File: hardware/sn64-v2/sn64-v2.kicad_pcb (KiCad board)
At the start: 6 copper layers, 104 x 64 mm, 180 parts, among them J1 Riser joint 2x20 2.00mm, J101 DX07S016JA3R1500, J2 SNES cartridge socket 62, U1 LFE5U-85F-8BG381I, U10 TLV62569DBVR, U11 AP2112K-2.5TRG1, U12 TPS2553DBVR, U2 W25Q128JVSIQ, U201 SN74ALVC164245DGGR, U202 SN74ALVC164245DGGR, U203 SN74ALVC164245DGGR, U204 SN74ALVC164245DGGR, U205 SN74LVC07APWR, U3 TPS3808G01DBVR, U4 USBLC6-2SC6, U6 TLA2528IRTER, U7 TPS2121RUXR, U8 TPS63070RNMR, U9 TLV62569DBVR, X1 27MHz 1631-27005-BTBEYA

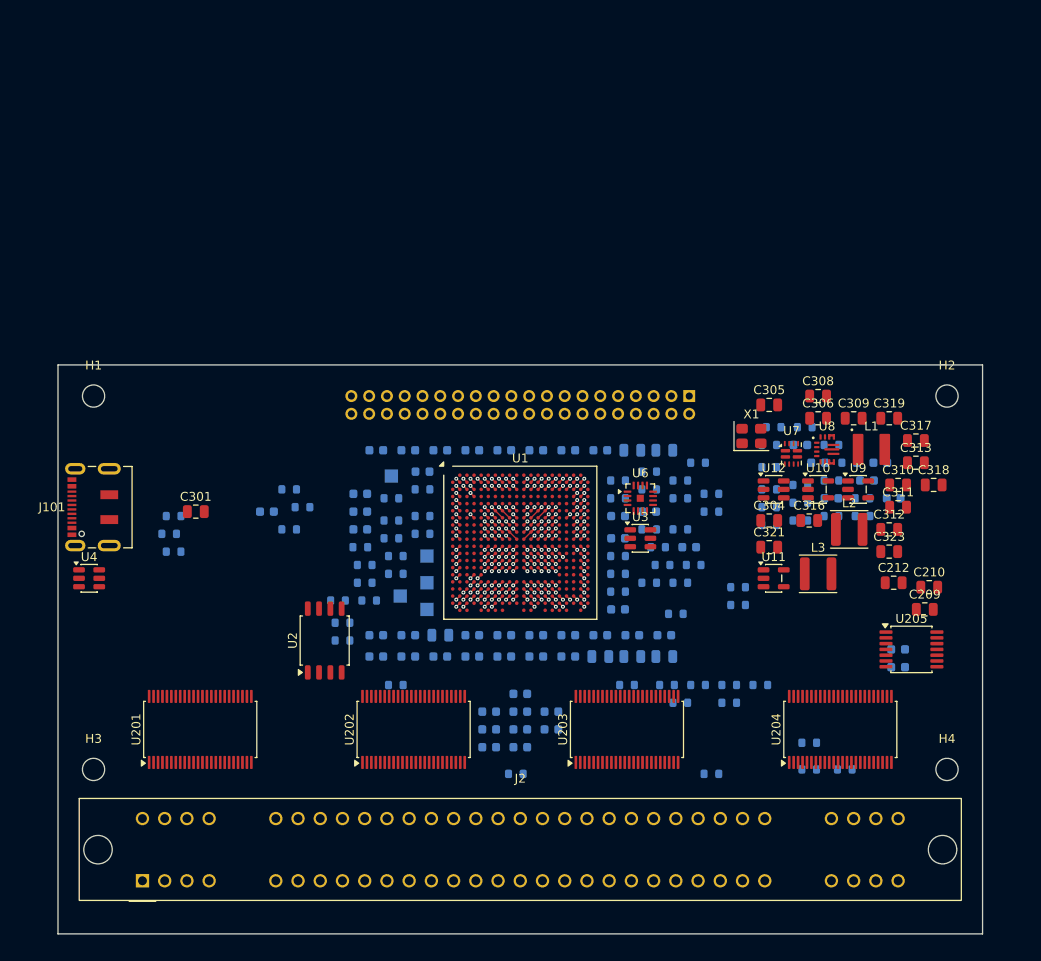
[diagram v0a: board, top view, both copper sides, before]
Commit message: v2 main board routed: 212/218 nets by one 40 s pass, planes and pours, DRC 0 errors; 7 hand items listed
Plane vias placed before routing (add_plane_vias_v2), 1.1 V island extended over its regulator on In4,
outer GND pours, renders and validation reports. Open items for hand routing in
hardware/sn64-v2/validation/pcb-open-connections.json. Work log and write-up updated.

Co-Authored-By: Claude Fable 5.1 <noreply@anthropic.com>
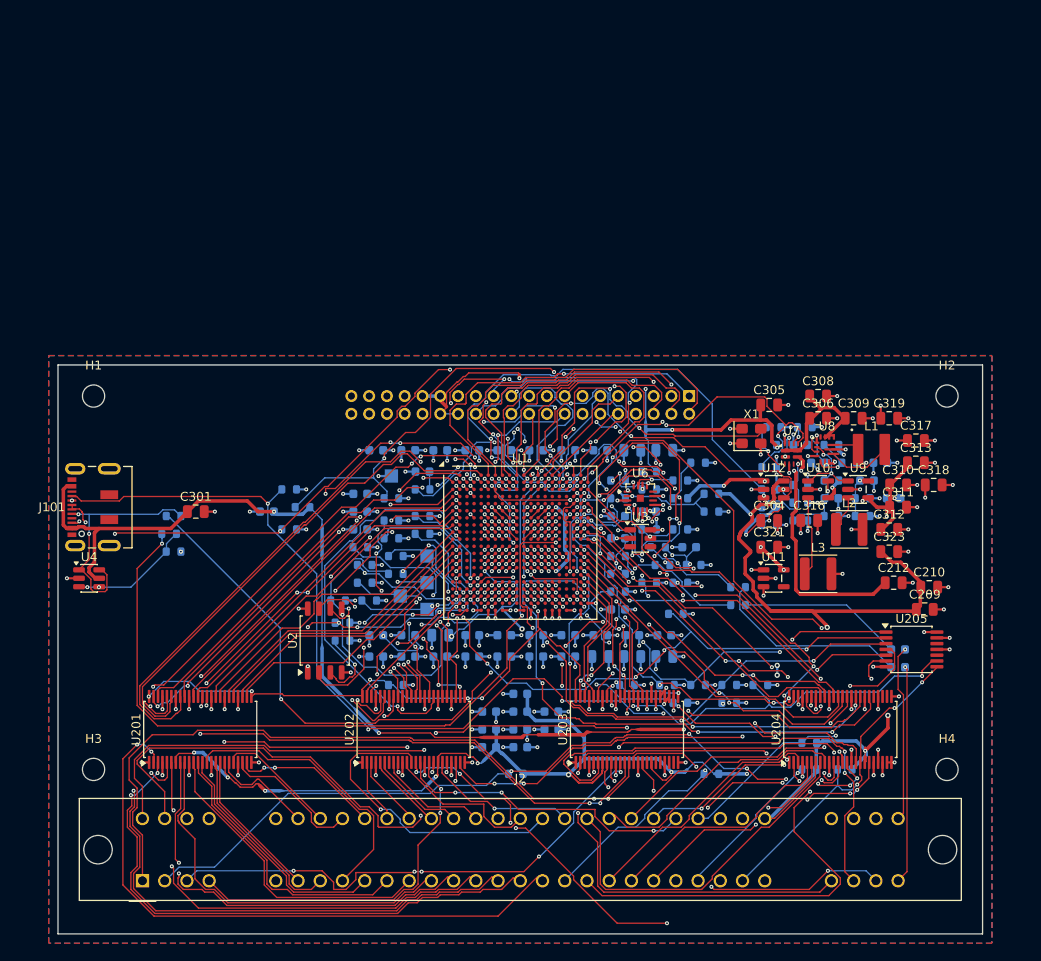
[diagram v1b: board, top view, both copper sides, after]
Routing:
- net SNES_5V_CART: track 0.00 -> 222.5 mm, vias 0 -> 12
- net GND: track 63.4 -> 261.4 mm, vias 94 -> 255
- net USB_VBUS: track 0.00 -> 143.6 mm, vias 0 -> 6
- net USB_CC2: track 0.00 -> 122.9 mm, vias 0 -> 7
- net FPGA_2V5: track 2.26 -> 111.2 mm, vias 4 -> 12
- net USB_CC1: track 0.00 -> 98.8 mm, vias 0 -> 12
- net FPGA_3V3: track 10.2 -> 104.7 mm, vias 18 -> 99
- net SNES_EXPAND: track 0.00 -> 91.1 mm, vias 0 -> 7
- net HOST_3V3: track 0.00 -> 88.9 mm, vias 0 -> 6
- net USB_DP_F: track 0.57 -> 87.9 mm, vias 1 -> 3
- net CTL_OE_N: track 0.57 -> 79.3 mm, vias 1 -> 7
- net SNES_SYSTEM_CLK: track 0.00 -> 78.1 mm, vias 0 -> 2
- net USB_DN_F: track 0.57 -> 77.3 mm, vias 1 -> 4
- net CIC_DATA0_OD: track 0.57 -> 72.2 mm, vias 1 -> 6
- net SNES_A0: track 0.00 -> 69.6 mm, vias 0 -> 2
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- added copper zone on B.Cu, net GND
- added copper zone on F.Cu, net GND

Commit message: v2 single board: routed board, schematic with the N64 edge, validation reports, renders and notes
Co-Authored-By: Claude Fable 5.1 <noreply@anthropic.com>
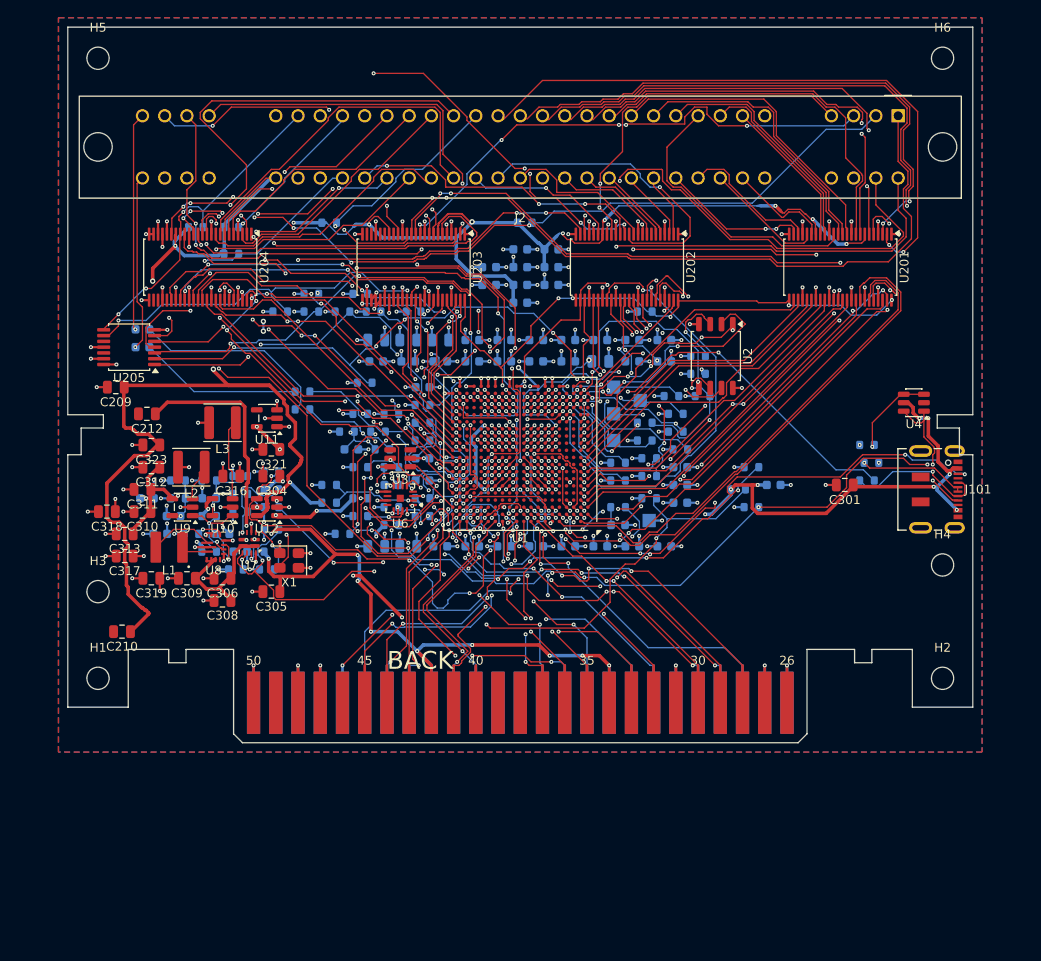
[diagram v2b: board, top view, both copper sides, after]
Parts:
- added H5: MountingHole_2.5mm, MountingHole_2.5mm, F.Cu at (-47.5, -66.5)
- added H6: MountingHole_2.5mm, MountingHole_2.5mm, F.Cu at (47.5, -66.5)
- J1: value Riser joint 2x20 2.00mm -> N64 cartridge edge; footprint PinSocket_2x20_P2.00mm_Vertical -> N64_Edge_SC64_Reference; moved to F.Cu
- moved R207 95.1 mm to (-36.5, -47.5), turned to 0 degrees
- moved U4 94.8 mm to (44.3, -27.8), turned to 180 degrees
- moved C209 94.4 mm to (-45.5, -29.5), turned to 180 degrees
- moved U205 94.3 mm to (-44.0, -34.0), turned to 180 degrees
- moved J101 93.6 mm to (46.2, -18.0), turned to -90 degrees
- moved C36 93.1 mm to (-42.5, -36.0), turned to 0 degrees
- moved C318 93.0 mm to (-46.5, -15.5), turned to 180 degrees
- moved C38 91.5 mm to (-42.5, -34.0), turned to 0 degrees
- moved C210 90.9 mm to (-44.8, -2.00), turned to 180 degrees
- moved C317 89.9 mm to (-44.5, -10.5), turned to 180 degrees
- moved C313 89.4 mm to (-44.5, -13.0), turned to 180 degrees
- moved R206 89.1 mm to (-32.5, -47.5), turned to 0 degrees
- moved U201 88.8 mm to (36.0, -43.0), turned to -90 degrees
- moved U204 88.8 mm to (-36.0, -43.0), turned to -90 degrees
- moved C212 86.1 mm to (-42.0, -26.5), turned to 180 degrees
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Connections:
- J1 pad 1: N64_AD0 -> GND
- J1 pad 10: N64_AD9 -> N64_READ_N
- J1 pad 11: N64_AD10 -> N64_AD11
- J1 pad 12: N64_AD11 -> N64_AD10
- J1 pad 13: N64_AD12 -> (no net)
- J1 pad 14: N64_AD13 -> (no net)
- J1 pad 15: N64_AD14 -> N64_AD9
- J1 pad 16: N64_AD15 -> N64_AD8
- J1 pad 17: N64_ALE_L -> HOST_3V3
- J1 pad 18: N64_ALE_H -> N64_CIC_DATA
- J1 pad 19: N64_READ_N -> N64_PIF_CLK
- J1 pad 2: N64_AD1 -> GND
- J1 pad 20: N64_WRITE_N -> N64_RESET_N
- J1 pad 21: N64_RESET_N -> N64_JOYBUS
- J1 pad 22: N64_NMI_N -> GND
- J1 pad 23: N64_INT_N -> GND
- J1 pad 24: N64_CIC_CLK -> (no net)
- J1 pad 25: N64_CIC_DATA -> GND
- J1 pad 26: N64_PIF_CLK -> GND
- J1 pad 27: N64_JOYBUS -> GND
- J1 pad 28: HOST_3V3 -> N64_AD0
- J1 pad 29: HOST_3V3 -> N64_AD1
- J1 pad 3: N64_AD2 -> N64_AD15
- J1 pad 30: HOST_3V3 -> N64_AD2
- J1 pad 31: HOST_3V3 -> GND
- J1 pad 32: GND -> N64_AD3
- J1 pad 33: GND -> N64_ALE_L
- J1 pad 34: GND -> HOST_3V3
- J1 pad 35: GND -> N64_ALE_H
- J1 pad 36: GND -> N64_AD4
- J1 pad 37: GND -> N64_AD5
- J1 pad 38: GND -> (no net)
- J1 pad 39: GND -> (no net)
- J1 pad 4: N64_AD3 -> N64_AD14
- J1 pad 40: GND -> N64_AD6
- J1 pad 5: N64_AD4 -> N64_AD13
- J1 pad 6: N64_AD5 -> GND
- J1 pad 7: N64_AD6 -> N64_AD12
- J1 pad 8: N64_AD7 -> N64_WRITE_N
- J1 pad 9: N64_AD8 -> HOST_3V3
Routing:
- net USB_DP_F: track 87.9 -> 0.00 mm, vias 3 -> 1
- net GND: track 261.4 -> 308.1 mm, vias 255 -> 258
- net OSC_27: track 36.6 -> 82.7 mm, vias 4 -> 5
- net N64_AD13: track 7.73 -> 41.5 mm, vias 1 -> 6
- net USB_CC2: track 122.9 -> 91.1 mm, vias 7 -> 10
- net N64_AD11: track 8.29 -> 37.2 mm, vias 1 -> 5
- net SNES_5V_CART: track 222.5 -> 250.8 mm
- net HOST_3V3: track 88.9 -> 116.0 mm, vias 6 -> 13
- net N64_AD12: track 9.65 -> 33.4 mm, vias 1 -> 3
- net N64_AD7: track 0.84 -> 24.3 mm, vias 1 -> 3
- net N64_AD15: track 14.6 -> 37.6 mm
- net N64_WRITE_N: track 8.05 -> 29.6 mm, vias 2 -> 4
- net N64_AD10: track 10.7 -> 31.6 mm, vias 1 -> 4
- net USB_VBUS: track 143.6 -> 123.1 mm, vias 6 -> 12
- net CART_5V_EN: track 57.8 -> 37.6 mm, vias 4 -> 7
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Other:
- board size 104 x 64 mm -> 101.8 x 80.5 mm

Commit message: v2 board refitted to the tower shell: SNES socket straddling the top edge, USB-C above the console
- New footprint SN64_V2:SNES_Slot_Console_Straddle (pins 1-31 on B.Cu, the face toward the
  front of the console; 32-62 on F.Cu) with a 3D model of the eared socket; generator and
  schematic point J2 at it (schematic diff: J2 footprint and note only).
- refit_tower_v2.py: clear (old socket, copper above the translators, USB-C nets cut at the
  old connector, dangling trim), place (outline 111 mm at the USB-C, 88 mm neck, J2 on the
  top edge, USB-C + ESD + VBUS cap at 50 mm, holes moved, planes enlarged, existing copper
  locked), unlock. KiCadRoutingTools routed 64/64 nets with nothing broken.
- DRC (board rules): 5 single-spoke thermal reliefs, 6 known open items; ERC unchanged.
- Fit check: the KiCad STEP with all part models has no interference with the shell.

Co-Authored-By: Claude Opus 5.5 <noreply@anthropic.com>
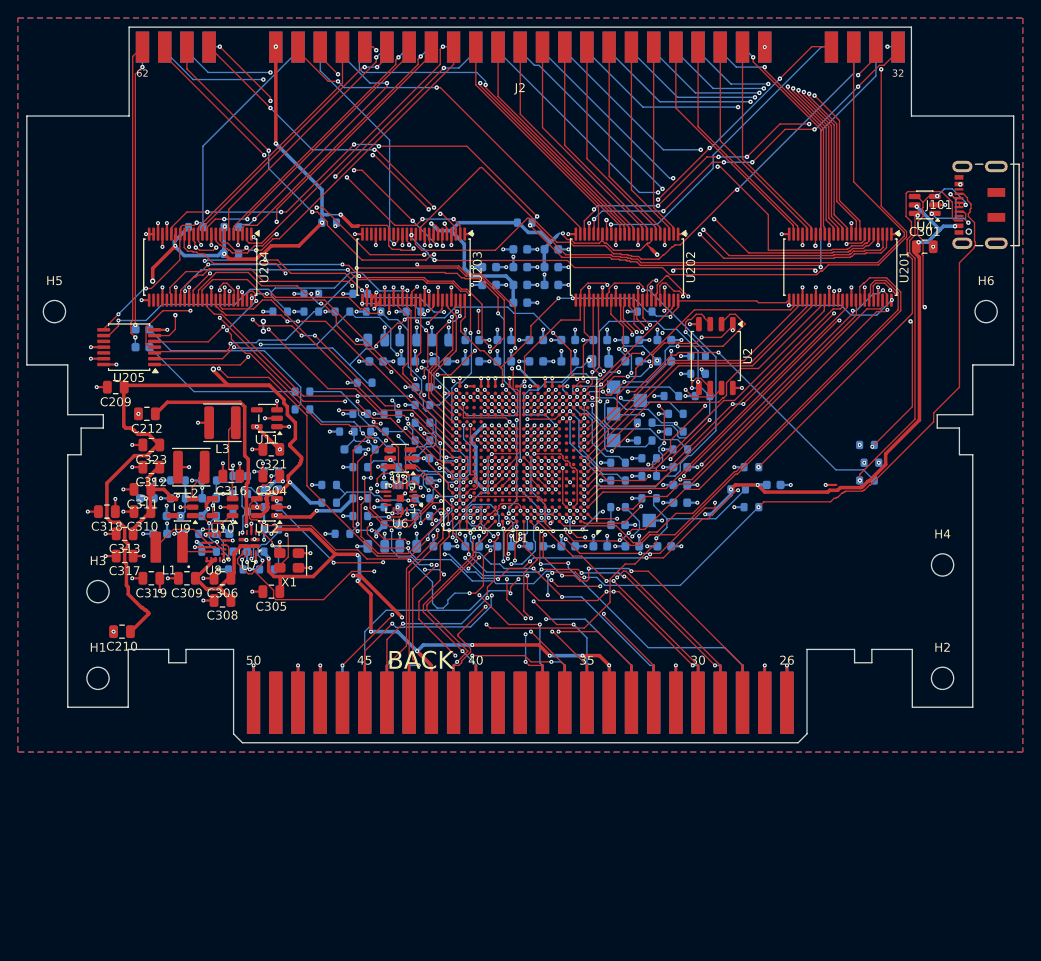
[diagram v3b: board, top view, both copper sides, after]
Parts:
- J2: footprint SNES_Slot_Console_7mm -> SN64_V2:SNES_Slot_Console_Straddle
- moved J101 32.6 mm to (52.4, -50.0), turned to 90 degrees
- moved H5 28.9 mm to (-52.4, -38.0)
- moved H6 28.9 mm to (52.4, -38.0)
- moved C301 28.3 mm to (45.5, -45.3), turned to 0 degrees
- moved U4 22.3 mm to (45.5, -50.0)
- moved J2 13.5 mm to (0.00, -70.0), turned to 0 degrees
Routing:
- net USB_CC2: track 91.1 -> 115.4 mm, vias 10 -> 8
- net SNES_PA7: track 63.9 -> 84.9 mm, vias 3 -> 0
- net SNES_EXPAND: track 91.1 -> 111.9 mm
- net USB_DN: track 26.3 -> 45.3 mm, vias 2 -> 5
- net USB_DP: track 23.4 -> 40.6 mm, vias 2 -> 6
- net USB_CC1: track 105.2 -> 121.4 mm, vias 12 -> 11
- net SNES_A16: track 6.51 -> 21.3 mm
- net SNES_A18: track 8.02 -> 22.8 mm
- net SNES_AUDIO_R_IN: track 19.8 -> 34.5 mm
- net SNES_A17: track 7.68 -> 22.1 mm
- net SNES_A2: track 61.4 -> 47.2 mm
- net SNES_A0: track 69.6 -> 55.3 mm
- net SNES_D0: track 47.1 -> 33.6 mm, vias 2 -> 1
- net USB_VBUS: track 123.1 -> 136.3 mm, vias 12 -> 11
- net SNES_A19: track 10.8 -> 23.6 mm
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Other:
- board size 101.8 x 80.5 mm -> 111 x 80.5 mm
